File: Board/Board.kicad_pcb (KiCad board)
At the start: 2 copper layers, 12 parts, among them Q1 Q_PNP_BCEC, U1 ADAU1701

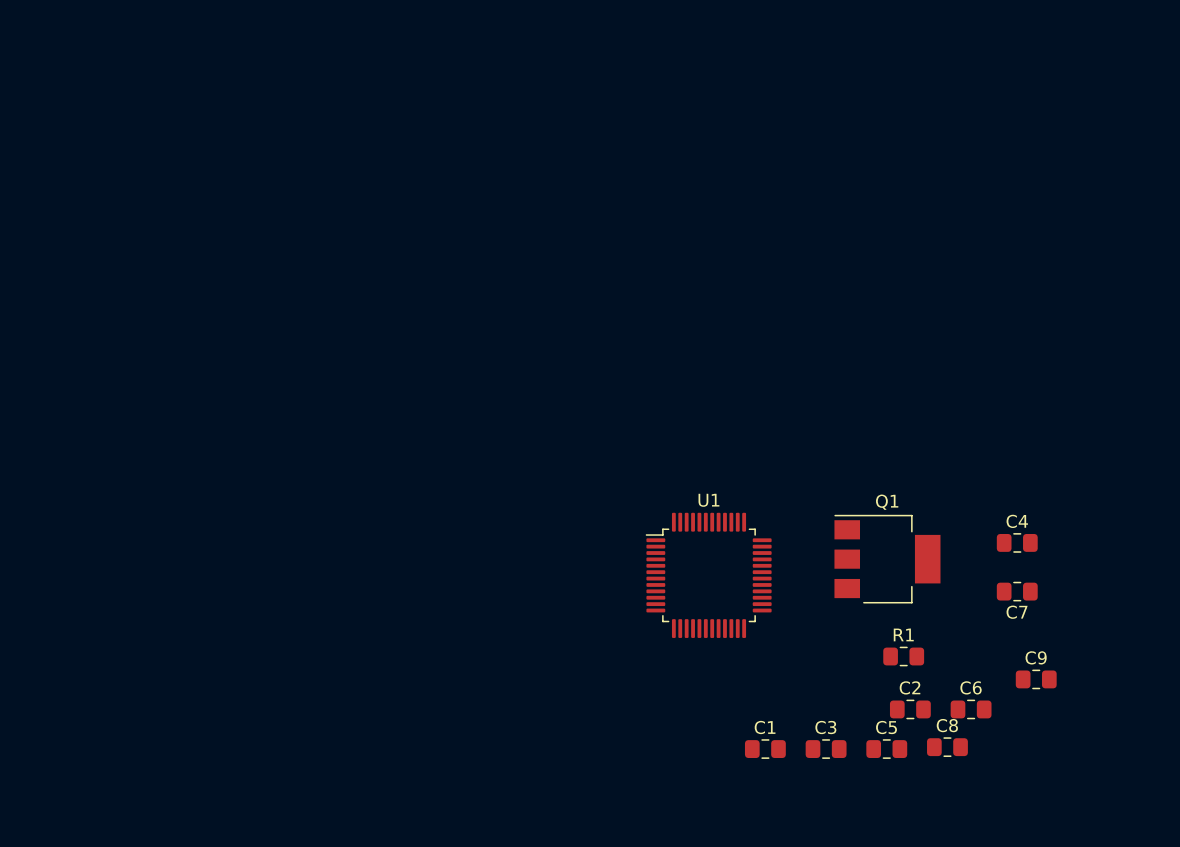
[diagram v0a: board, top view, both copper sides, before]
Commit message: added datasheets
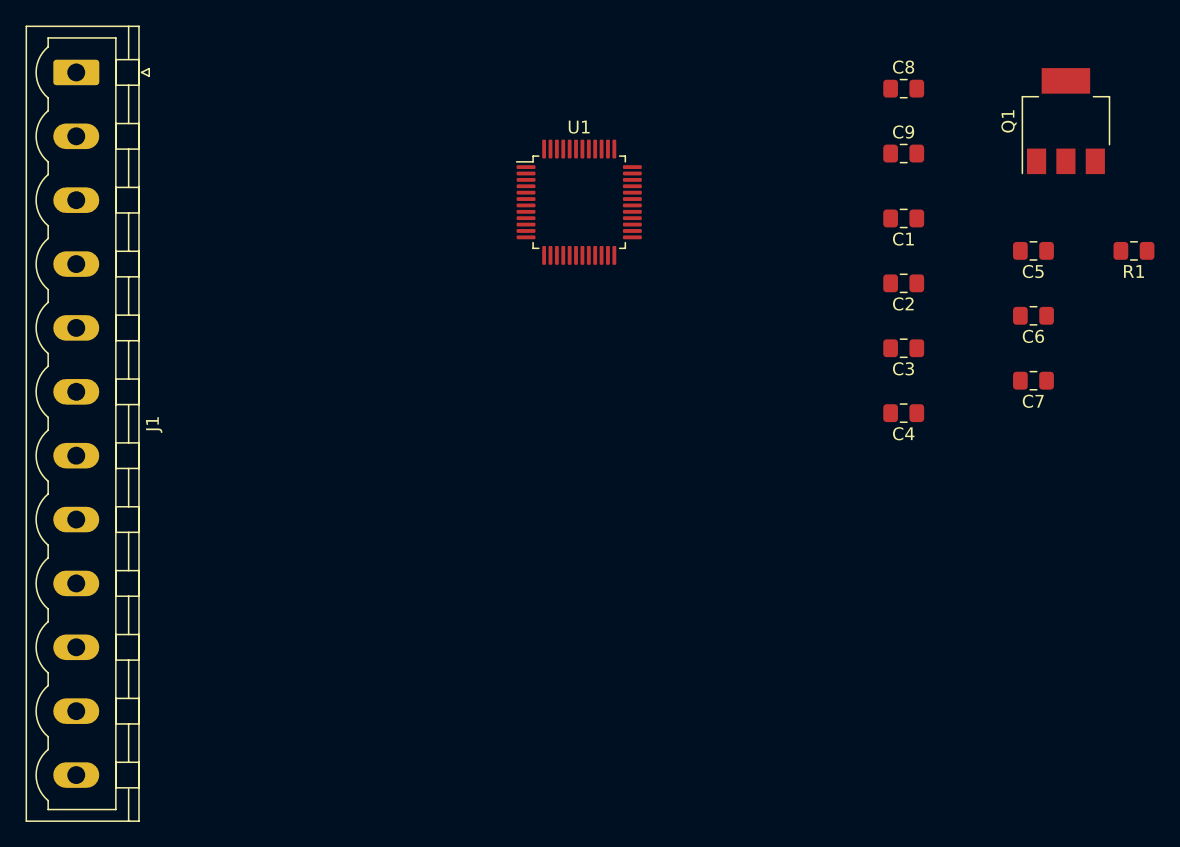
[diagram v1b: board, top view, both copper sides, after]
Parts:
- added J1: Conn_01x12_Male, Connector_Phoenix_MSTB:PhoenixContact_MSTBVA_2,5_12-G_1x12_P5.00mm_Vertical, F.Cu at (19.1, 38.1)
- moved C8 51.7 mm to (83.8, 39.4)
- moved C1 42.9 mm to (83.8, 49.5), turned to 180 degrees
- moved C9 42.5 mm to (83.8, 44.5)
- moved C5 40.7 mm to (94.0, 52.1), turned to 180 degrees
- moved Q1 37.0 mm to (96.5, 41.9), turned to 90 degrees
- moved R1 36.5 mm to (101.8, 52.1), turned to 180 degrees
- moved C2 33.4 mm to (83.8, 54.6), turned to 180 degrees
- moved C3 32.0 mm to (83.8, 59.7), turned to 180 degrees
- moved C6 31.2 mm to (94.0, 57.1), turned to 180 degrees
- moved U1 30.9 mm to (58.4, 48.3)
- moved C7 16.6 mm to (94.0, 62.2)
- moved C4 13.5 mm to (83.8, 64.8), turned to 180 degrees

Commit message: did some more stuff
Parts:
- added C10: 100nF, Capacitor_SMD:C_0805_2012Metric_Pad1.15x1.40mm_HandSolder, F.Cu at (137.1, 32.1)
- added C11: 100nF, Capacitor_SMD:C_0805_2012Metric_Pad1.15x1.40mm_HandSolder, F.Cu at (146.9, 23.8)
- added J2: Audio In, Connector_Phoenix_MSTB:PhoenixContact_MSTBA_2,5_3-G_1x03_P5.00mm_Horizontal, F.Cu at (69.8, 36.9)
- added R2: 18k0, Resistor_SMD:R_0805_2012Metric_Pad1.15x1.40mm_HandSolder, F.Cu at (102.8, 34.9)
- added R3: 18k0, Resistor_SMD:R_0805_2012Metric_Pad1.15x1.40mm_HandSolder, F.Cu at (98.0, 34.9)
- added R4: 100, Resistor_SMD:R_0805_2012Metric_Pad1.15x1.40mm_HandSolder, F.Cu at (78.2, 64.2)
- added R5: 1k00, Resistor_SMD:R_0805_2012Metric_Pad1.15x1.40mm_HandSolder, F.Cu at (151.7, 29.7)
- added Y1: Crystal_Small, ECS-122.8-20-3X-EN-TR:XTAL_ECS-122.8-20-3X-EN-TR, F.Cu at (70.5, 65.5)
- C1, C2: value 100nF -> 22pF
- C4, C5, C8: value 10nF -> 100nF
- C6, C7, C9: value 100nF -> 10nF
- R1: value 1k00 -> 18k
- moved C3 72.7 mm to (151.3, 32.7), turned to 0 degrees
- moved C4 70.5 mm to (146.6, 32.7), turned to 0 degrees
- moved C7 69.3 mm to (151.7, 23.8), turned to 0 degrees
- moved C8 64.3 mm to (146.9, 26.8)
- moved C5 63.0 mm to (151.7, 26.8), turned to 0 degrees
- moved C6 59.6 mm to (146.9, 29.7), turned to 0 degrees
- moved C9 59.3 mm to (141.8, 32.1)
- moved J1 51.6 mm to (69.8, 28.6), turned to 0 degrees
- moved Q1 45.8 mm to (139.6, 26.5), turned to 0 degrees
- moved U1 32.9 mm to (90.0, 39.1)
- moved C1 23.3 mm to (72.4, 69.8), turned to 0 degrees
- moved C2 22.2 mm to (67.6, 69.8), turned to 0 degrees
- moved R1 18.1 mm to (107.5, 34.9), turned to 0 degrees
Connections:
- C1 pad 1: VDD -> GND
- C1 pad 2: GND -> Net-(C1-Pad2)
- C2 pad 1: VDD -> GND
- C2 pad 2: GND -> /oscillator/MCLKI
- C5 pad 1: GND -> VDD
- C5 pad 2: Net-(C5-Pad2) -> GND
- C6 pad 1: GND -> VDD
- C6 pad 2: Net-(C5-Pad2) -> GND
- C7 pad 2: Net-(C5-Pad2) -> VDD
- C9 pad 2: VDD -> /power/DVDD
- Q1 pad 1: Net-(Q1-Pad1) -> /power/VDRIVE
- Q1 pad 2: Net-(C5-Pad2) -> /power/DVDD
- Q1 pad 4: Net-(C5-Pad2) -> /power/DVDD
- R1 pad 1: VDD -> Net-(R1-Pad1)
- R1 pad 2: Net-(Q1-Pad1) -> GND
- U1 pad 1: Net-(U1-Pad1) -> GND
- U1 pad 12: Net-(U1-Pad12) -> GND
- U1 pad 13: Net-(C5-Pad2) -> /power/DVDD
- U1 pad 17: Net-(Q1-Pad1) -> /power/VDRIVE
- U1 pad 24: Net-(C5-Pad2) -> /power/DVDD
- U1 pad 25: Net-(U1-Pad12) -> GND
- U1 pad 3: Net-(U1-Pad3) -> Net-(R1-Pad1)
- U1 pad 30: Net-(U1-Pad30) -> GND
- U1 pad 31: Net-(U1-Pad31) -> /oscillator/OSCO
- U1 pad 32: Net-(U1-Pad32) -> /oscillator/MCLKI
- U1 pad 33: Net-(U1-Pad33) -> GND
- U1 pad 37: Net-(U1-Pad1) -> GND
- U1 pad 42: Net-(U1-Pad1) -> GND

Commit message: more improvements
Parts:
- added C12: 47uF, Capacitor_SMD:C_0805_2012Metric_Pad1.15x1.40mm_HandSolder, F.Cu at (90.2, -23.7)
- added C13: 5n6F, Capacitor_SMD:C_0805_2012Metric_Pad1.15x1.40mm_HandSolder, F.Cu at (90.2, -26.6)
- added C14: 47uF, Capacitor_SMD:C_0805_2012Metric_Pad1.15x1.40mm_HandSolder, F.Cu at (124.8, -46.6)
- added C15: 5n6F, Capacitor_SMD:C_0805_2012Metric_Pad1.15x1.40mm_HandSolder, F.Cu at (120.0, -43.6)
- added C16: 47uF, Capacitor_SMD:C_0805_2012Metric_Pad1.15x1.40mm_HandSolder, F.Cu at (104.7, -23.7)
- added C17: 5n6F, Capacitor_SMD:C_0805_2012Metric_Pad1.15x1.40mm_HandSolder, F.Cu at (104.7, -26.6)
- added C18: 47uF, Capacitor_SMD:C_0805_2012Metric_Pad1.15x1.40mm_HandSolder, F.Cu at (120.0, -34.1)
- added C19: 5n6F, Capacitor_SMD:C_0805_2012Metric_Pad1.15x1.40mm_HandSolder, F.Cu at (120.0, -37.1)
- added J3: MP 3-5, 691213710003:691213710003, F.Cu at (89.1, -55.2)
- added J4: MP 6-8, 691213710003:691213710003, F.Cu at (71.9, -45.3)
- added J5: MP 9-11, 691213710003:691213710003, F.Cu at (71.9, -55.2)
- added R6: 560r, Resistor_SMD:R_0805_2012Metric_Pad1.15x1.40mm_HandSolder, F.Cu at (94.9, -26.6)
- added R7: 560r, Resistor_SMD:R_0805_2012Metric_Pad1.15x1.40mm_HandSolder, F.Cu at (120.0, -46.6)
- added R8: 560r, Resistor_SMD:R_0805_2012Metric_Pad1.15x1.40mm_HandSolder, F.Cu at (109.5, -26.6)
- added R9: 560r, Resistor_SMD:R_0805_2012Metric_Pad1.15x1.40mm_HandSolder, F.Cu at (124.8, -37.1)
- J1: value Conn_01x12_Male -> MP 0-2; footprint Connector_Phoenix_MSTB:PhoenixContact_MSTBVA_2,5_12-G_1x12_P5.00mm_Vertical -> 691213710003:691213710003
- J2: footprint Connector_Phoenix_MSTB:PhoenixContact_MSTBA_2,5_3-G_1x03_P5.00mm_Horizontal -> 691213710003:691213710003
- moved C1 133.6 mm to (124.8, -53.1)
- moved C2 133.6 mm to (120.0, -53.1)
- moved R4 133.6 mm to (130.6, -58.7)
- moved Y1 133.6 mm to (122.9, -57.4)
- moved C3 100.0 mm to (65.4, -18.4)
- moved R5 95.0 mm to (75.2, -26.6)
- moved C4 91.9 mm to (70.1, -18.4)
- moved C5 91.6 mm to (75.2, -23.7)
- moved J1 91.5 mm to (106.4, -55.2)
- moved C7 88.5 mm to (75.2, -20.7)
- moved Q1 87.7 mm to (67.9, -24.0)
- moved C6 87.5 mm to (80.0, -26.6)
- moved U1 84.7 mm to (103.1, -44.6)
- moved J2 84.5 mm to (89.1, -45.3)
- moved C8 83.8 mm to (80.0, -23.7)
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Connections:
- J2 pad 3: GND -> Net-(J2-Pad3)
- R2 pad 2: Net-(J2-Pad1) -> Net-(R2-Pad2)
- R3 pad 2: Net-(J2-Pad2) -> Net-(R3-Pad2)
- U1 pad 10: Net-(J1-Pad11) -> Net-(J1-Pad2)
- U1 pad 11: Net-(J1-Pad12) -> Net-(J1-Pad1)
- U1 pad 14: Net-(J1-Pad5) -> Net-(J4-Pad2)
- U1 pad 15: Net-(J1-Pad6) -> Net-(J4-Pad1)
- U1 pad 16: Net-(J1-Pad2) -> Net-(J5-Pad2)
- U1 pad 19: Net-(J1-Pad1) -> Net-(J5-Pad3)
- U1 pad 26: Net-(J1-Pad3) -> Net-(J5-Pad1)
- U1 pad 27: Net-(J1-Pad4) -> Net-(J4-Pad3)
- U1 pad 28: Net-(J1-Pad9) -> Net-(J3-Pad1)
- U1 pad 29: Net-(J1-Pad10) -> Net-(J1-Pad3)
- U1 pad 43: Net-(U1-Pad43) -> /output filter  4/In
- U1 pad 44: Net-(U1-Pad44) -> /output filter 3/In
- U1 pad 45: Net-(U1-Pad45) -> /output filter 2/In
- U1 pad 46: Net-(U1-Pad46) -> /output filter 1/In
- U1 pad 8: Net-(J1-Pad8) -> Net-(J3-Pad2)
- U1 pad 9: Net-(J1-Pad7) -> Net-(J3-Pad3)
